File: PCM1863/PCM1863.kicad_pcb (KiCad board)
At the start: 2 copper layers, 70 x 45 mm, 47 parts, among them IC1 SN74AUC1G126DCKR, IC2 NCP163ASN330T1G, IC3 NCP163ASN330T1G, J1 Conn_01x10_Male, J2 Conn_01x10_Male, J3 Conn_01x10_Male, J4 USB_B_Micro, U1 PCM1863, Y1 ASE-24.000MHZ-ET, Y2 ASE-22.000MHZ-ET

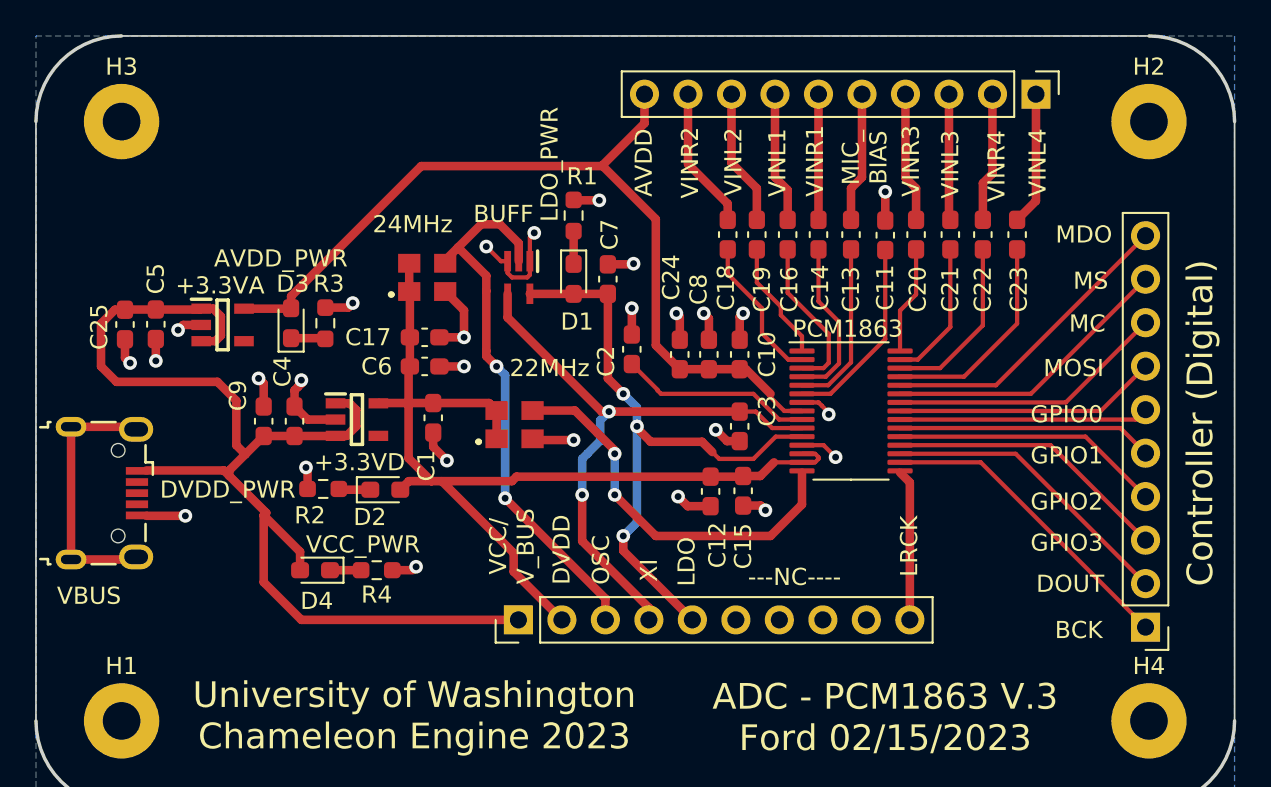
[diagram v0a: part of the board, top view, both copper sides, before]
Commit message: fix analog too close to digital
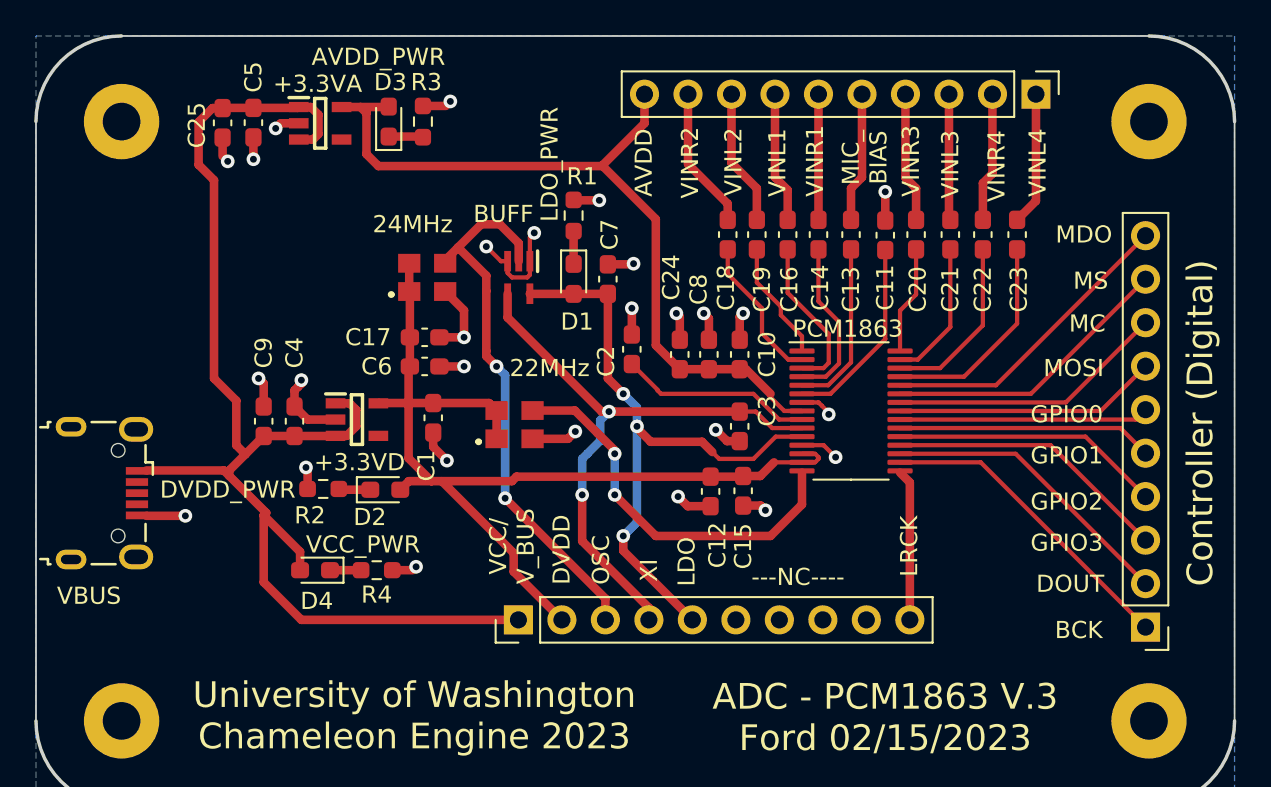
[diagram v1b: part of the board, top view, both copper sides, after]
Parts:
- moved C5 13.1 mm to (127.7, 120.1)
- moved D3 13.1 mm to (135.6, 120.0)
- moved IC3 13.1 mm to (131.6, 120.1)
- moved R3 13.1 mm to (137.6, 120.0)
- moved C25 13.1 mm to (125.9, 120.1)
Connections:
- J4 pad 6: unconnected-(J4-Pad6) -> GND
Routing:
- net unconnected-(J4-Pad6): track 15.3 -> 0.00 mm
- net VCC: track 67.7 -> 73.6 mm
- net AVDD: track 52.3 -> 47.3 mm

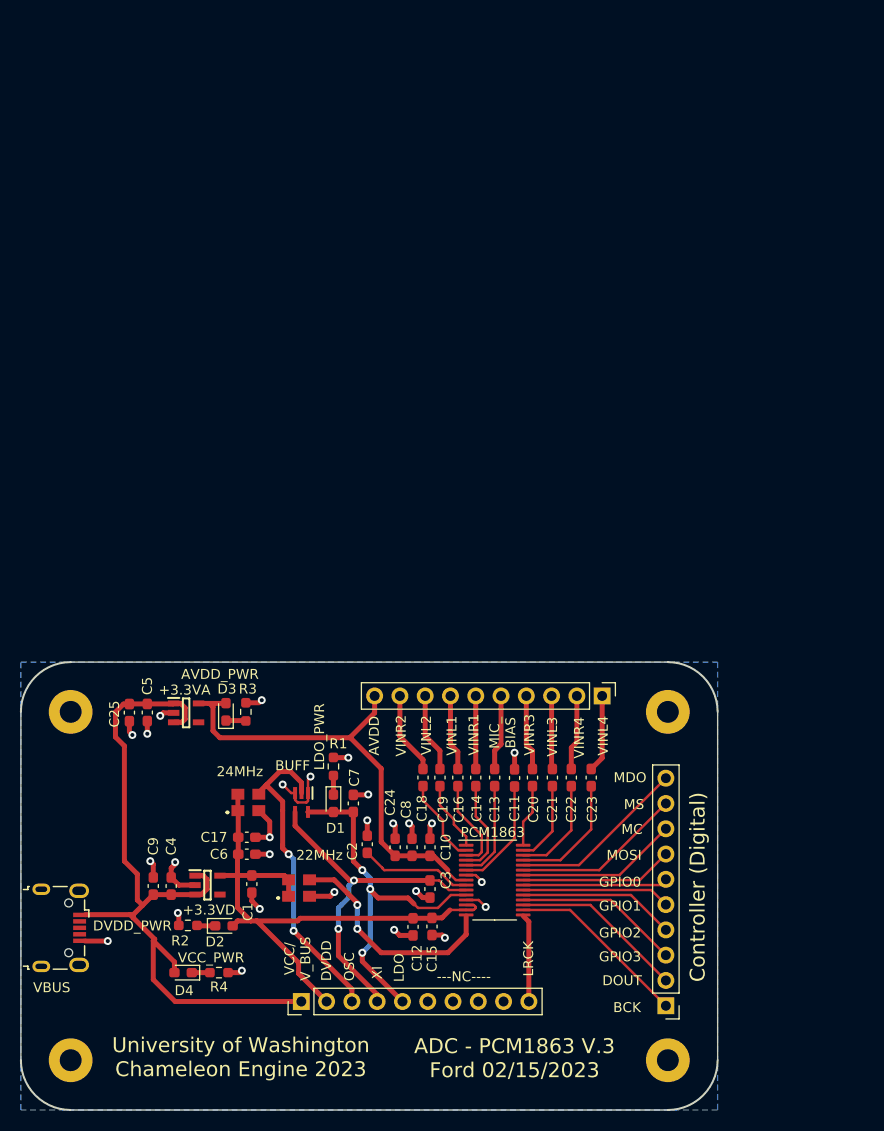
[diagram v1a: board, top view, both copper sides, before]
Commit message: schematic updates for ADC
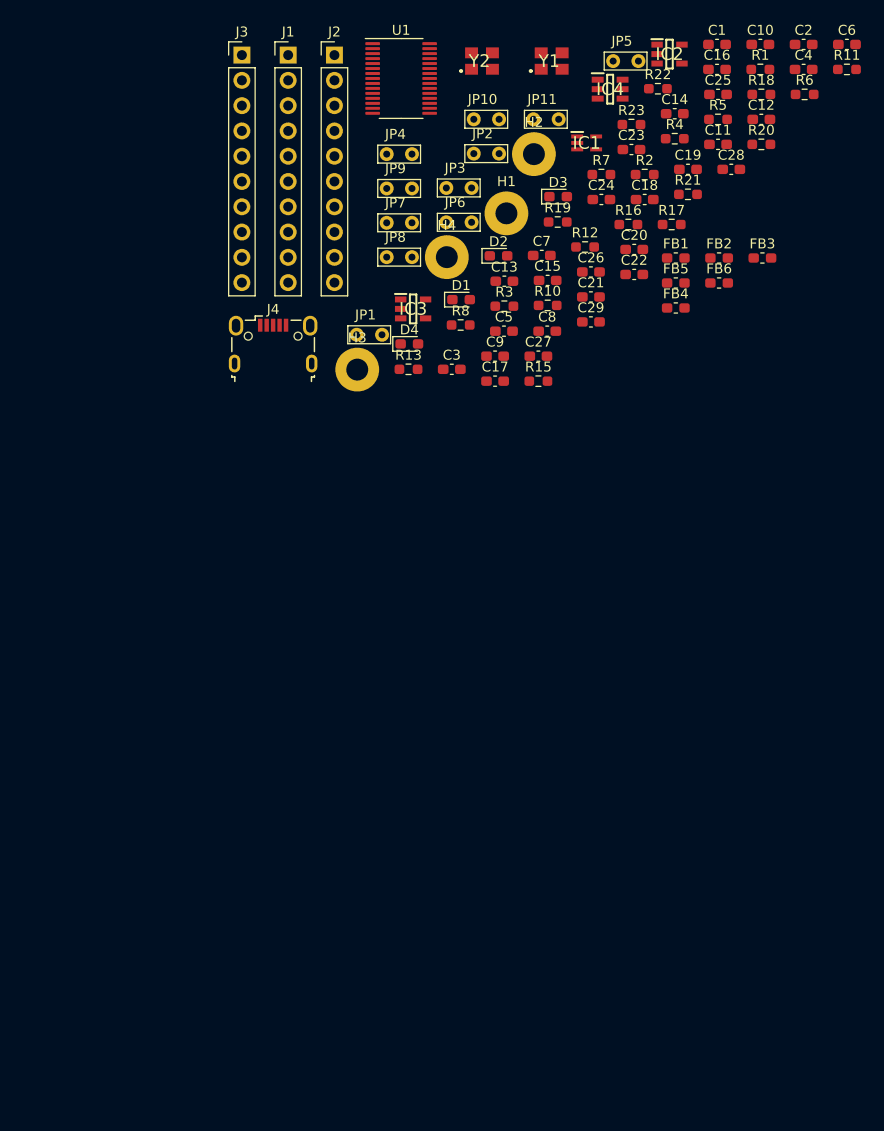
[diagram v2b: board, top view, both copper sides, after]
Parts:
- added C26: 10uF-16V, Capacitor_SMD:C_0603_1608Metric_Pad1.08x0.95mm_HandSolder, F.Cu at (172.3, 75.8)
- added C27: 10uF-16V, Capacitor_SMD:C_0603_1608Metric_Pad1.08x0.95mm_HandSolder, F.Cu at (167.0, 84.3)
- added C28: 0.1uF-16V, Capacitor_SMD:C_0603_1608Metric_Pad1.08x0.95mm_HandSolder, F.Cu at (186.4, 65.5)
- added C29: 0.1uF-16V, Capacitor_SMD:C_0603_1608Metric_Pad1.08x0.95mm_HandSolder, F.Cu at (172.3, 80.8)
- added FB1: FerriteBead, Inductor_SMD:L_0603_1608Metric_Pad1.05x0.95mm_HandSolder, F.Cu at (180.8, 74.4)
- added FB2: FerriteBead, Inductor_SMD:L_0603_1608Metric_Pad1.05x0.95mm_HandSolder, F.Cu at (185.2, 74.4)
- added FB3: FerriteBead, Inductor_SMD:L_0603_1608Metric_Pad1.05x0.95mm_HandSolder, F.Cu at (189.5, 74.4)
- added FB4: FerriteBead, Inductor_SMD:L_0603_1608Metric_Pad1.05x0.95mm_HandSolder, F.Cu at (180.8, 79.4)
- added FB5: FerriteBead, Inductor_SMD:L_0603_1608Metric_Pad1.05x0.95mm_HandSolder, F.Cu at (180.8, 76.9)
- added FB6: FerriteBead, Inductor_SMD:L_0603_1608Metric_Pad1.05x0.95mm_HandSolder, F.Cu at (185.2, 76.9)
- added IC4: TXB0101DBVT, custom_lib:SOT95P280X145-6N, F.Cu at (174.2, 57.4)
- added JP1: Jumper_2_Open, custom_lib:TestPoint_Bridge_Pitch2.54mm_Drill0.7mm, F.Cu at (147.5, 80.9)
- added JP10: Jumper_2_Open, custom_lib:TestPoint_Bridge_Pitch2.54mm_Drill0.7mm, F.Cu at (159.3, 59.3)
- added JP11: Jumper_2_Open, custom_lib:TestPoint_Bridge_Pitch2.54mm_Drill0.7mm, F.Cu at (165.3, 59.3)
- added JP2: Jumper_2_Open, custom_lib:TestPoint_Bridge_Pitch2.54mm_Drill0.7mm, F.Cu at (159.3, 62.7)
- added JP3: Jumper_2_Open, custom_lib:TestPoint_Bridge_Pitch2.54mm_Drill0.7mm, F.Cu at (156.5, 66.2)
- added JP4: Jumper_2_Open, custom_lib:TestPoint_Bridge_Pitch2.54mm_Drill0.7mm, F.Cu at (150.6, 62.8)
- added JP5: Jumper_2_Bridged, custom_lib:TestPoint_Bridge_Pitch2.54mm_Drill0.7mm, F.Cu at (173.3, 53.4)
- added JP6: Jumper_2_Open, custom_lib:TestPoint_Bridge_Pitch2.54mm_Drill0.7mm, F.Cu at (156.5, 69.6)
- added JP7: Jumper_2_Bridged, custom_lib:TestPoint_Bridge_Pitch2.54mm_Drill0.7mm, F.Cu at (150.6, 69.7)
- added JP8: Jumper_2_Open, custom_lib:TestPoint_Bridge_Pitch2.54mm_Drill0.7mm, F.Cu at (150.6, 73.1)
- added JP9: Jumper_2_Open, custom_lib:TestPoint_Bridge_Pitch2.54mm_Drill0.7mm, F.Cu at (150.6, 66.2)
- added R10: 2.2k, Resistor_SMD:R_0603_1608Metric_Pad0.98x0.95mm_HandSolder, F.Cu at (167.9, 79.2)
- added R11: 2.2k, Resistor_SMD:R_0603_1608Metric_Pad0.98x0.95mm_HandSolder, F.Cu at (198.0, 55.5)
- added R12: 100k, Resistor_SMD:R_0603_1608Metric_Pad0.98x0.95mm_HandSolder, F.Cu at (171.7, 73.3)
- added R13: 100k, Resistor_SMD:R_0603_1608Metric_Pad0.98x0.95mm_HandSolder, F.Cu at (153.9, 85.6)
- added R15: 2.2k, Resistor_SMD:R_0603_1608Metric_Pad0.98x0.95mm_HandSolder, F.Cu at (167.0, 86.8)
- added R16: 2.2k, Resistor_SMD:R_0603_1608Metric_Pad0.98x0.95mm_HandSolder, F.Cu at (176.0, 71.0)
- added R17: 100k, Resistor_SMD:R_0603_1608Metric_Pad0.98x0.95mm_HandSolder, F.Cu at (180.4, 71.0)
- added R18: 100k, Resistor_SMD:R_0603_1608Metric_Pad0.98x0.95mm_HandSolder, F.Cu at (189.4, 58.0)
- added R19: 2.2k, Resistor_SMD:R_0603_1608Metric_Pad0.98x0.95mm_HandSolder, F.Cu at (168.9, 70.8)
- added R20: 2.2k, Resistor_SMD:R_0603_1608Metric_Pad0.98x0.95mm_HandSolder, F.Cu at (189.4, 63.0)
- added R21: 100k, Resistor_SMD:R_0603_1608Metric_Pad0.98x0.95mm_HandSolder, F.Cu at (182.0, 68.0)
- added R22: 100k, Resistor_SMD:R_0603_1608Metric_Pad0.98x0.95mm_HandSolder, F.Cu at (179.0, 57.4)
- added R23: 4.99k, Resistor_SMD:R_0603_1608Metric_Pad0.98x0.95mm_HandSolder, F.Cu at (176.3, 61.0)
- added R5: 2.2k, Resistor_SMD:R_0603_1608Metric_Pad0.98x0.95mm_HandSolder, F.Cu at (185.0, 60.5)
- added R6: 2.2k, Resistor_SMD:R_0603_1608Metric_Pad0.98x0.95mm_HandSolder, F.Cu at (193.7, 58.0)
- added R7: 100k, Resistor_SMD:R_0603_1608Metric_Pad0.98x0.95mm_HandSolder, F.Cu at (173.3, 66.0)
- added R8: 100k, Resistor_SMD:R_0603_1608Metric_Pad0.98x0.95mm_HandSolder, F.Cu at (159.2, 81.1)
- C10, C15: value 0.1uF -> 0.1uF-16V
- C12, C14, C8: value 10uF -> 10uF-10V
- C13: value 0.1uF -> 0.1uF-50V
- C16: value 10uF -> 0.1uF-16V
- C18, C19, C20, C21, C22, C23: value 10uF -> 10uF-16V
- C2, C3: value 18pF -> 20pF-50V
- moved J3 104.6 mm to (137.2, 54.0), turned to 0 degrees
- moved C4 103.8 mm to (193.6, 55.5), turned to 0 degrees
- moved C6 101.3 mm to (198.0, 52.9), turned to 0 degrees
- moved C1 96.4 mm to (184.9, 52.9), turned to 0 degrees
- moved H1 95.7 mm to (163.8, 69.9)
- moved IC2 95.5 mm to (180.2, 53.9)
- moved R4 95.5 mm to (180.7, 62.4), turned to 0 degrees
- moved J1 95.1 mm to (141.9, 54.0), turned to 0 degrees
- moved C2 91.5 mm to (193.6, 52.9), turned to 0 degrees
- moved C12 88.4 mm to (189.4, 60.5), turned to 0 degrees
- moved R2 88.3 mm to (177.7, 66.0), turned to 0 degrees
- moved C10 87.2 mm to (189.3, 52.9), turned to 0 degrees
- moved C25 85.8 mm to (185.0, 58.0), turned to 0 degrees
- moved Y2 85.1 mm to (161.3, 54.6)
- moved H4 83.7 mm to (157.8, 74.3)
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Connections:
- C1 pad 2: GND -> GNDD
- C10 pad 1: GND -> GNDA
- C11 pad 1: GND -> GNDA
- C12 pad 2: GND -> GNDD
- C13 pad 1: /A5 -> GNDA
- C13 pad 2: Net-(C13-Pad2) -> MICBIAS
- C14 pad 1: /A4 -> LDO
- C14 pad 2: Net-(C14-Pad2) -> GNDD
- C15 pad 2: GND -> GNDD
- C16 pad 1: /A3 -> LDO
- C16 pad 2: Net-(C16-Pad2) -> GNDD
- C17 pad 2: GND -> GNDD
- C18 pad 1: /A2 -> VINR1
- C18 pad 2: Net-(C18-Pad2) -> /1R
- C19 pad 1: /A1 -> VINL1
- C19 pad 2: Net-(C19-Pad2) -> /1L
- C2 pad 1: GND -> GNDD
- C20 pad 1: /A17 -> VINR3
- C20 pad 2: Net-(C20-Pad2) -> /3R
- C21 pad 1: /A16 -> VINL3
- C21 pad 2: Net-(C21-Pad2) -> /3L
- C22 pad 1: /A15 -> VINR4
- C22 pad 2: Net-(C22-Pad2) -> /4R
- C23 pad 1: /A14 -> VINL4
- C23 pad 2: Net-(C23-Pad2) -> /4L
- C24 pad 1: GND -> GNDA
- C25 pad 2: GND -> GNDA
- C3 pad 1: GND -> GNDD
- C4 pad 2: GND -> GNDD
- C5 pad 2: GND -> GNDA
- C6 pad 1: GND -> GNDD
- C7 pad 2: GND -> GNDD
- C8 pad 1: GND -> GNDA
- C9 pad 2: GND -> GNDD
- IC1 pad 1: GND -> GNDD
- IC1 pad 3: GND -> GNDD
- IC2 pad 2: GND -> GNDD
- J1 pad 8: unconnected-(J1-Pad8) -> XO_BUFF
- J1 pad 9: unconnected-(J1-Pad9) -> SCKI(3.3V)
- J2 pad 1: /A14 -> /1R
- J2 pad 2: /A15 -> /1L
- J2 pad 3: /A16 -> /2R
- J2 pad 4: /A17 -> /2L
- J2 pad 5: /A5 -> /3R
- J2 pad 6: /A4 -> /3L
- J2 pad 7: /A3 -> /4R
- J2 pad 8: /A1 -> /4L
- J2 pad 9: /A2 -> MICBIAS
- J3 pad 10: /A13 -> /INT/GPIO3/INTC
- J3 pad 3: /A6 -> /MDO
- J3 pad 4: /A7 -> /MD1/MS/AD
- J3 pad 5: /A8 -> /MD3/MC/SCL
- J3 pad 6: /A9 -> /DOUT2/MD2/MOSI/SDA
- J3 pad 7: /A10 -> /MD4/MISO/GPIO0
- J3 pad 8: /A11 -> /MD5/GPIO1/INTA/DMIN
- J3 pad 9: /A12 -> /MD6/GPIO2/INTB/DMCLK
- J4 pad 5: GND -> GNDA
- J4 pad 6: GND -> unconnected-(J4-Pad6)
- R1 pad 2: GND -> GNDD
- R2 pad 2: GND -> GNDD
- R3 pad 2: GND -> GNDA
- R4 pad 1: GND -> GNDA
- U1 pad 1: Net-(C19-Pad2) -> /2L
- U1 pad 12: GND -> GNDD
- U1 pad 19: /A6 -> /INT/GPIO3/INTC
- U1 pad 2: Net-(C18-Pad2) -> /2R
- U1 pad 20: /A7 -> /MD6/GPIO2/INTB/DMCLK
- U1 pad 21: /A8 -> /MD5/GPIO1/INTA/DMIN
- U1 pad 22: /A9 -> /MD4/MISO/GPIO0
- U1 pad 23: /A10 -> /DOUT2/MD2/MOSI/SDA
- U1 pad 24: /A11 -> /MD3/MC/SCL
- U1 pad 25: /A12 -> /MD1/MS/AD
- U1 pad 26: /A13 -> /MDO
- U1 pad 27: Net-(C23-Pad2) -> /4L
- U1 pad 28: Net-(C22-Pad2) -> /4R
- U1 pad 29: Net-(C21-Pad2) -> /3L
- U1 pad 3: Net-(C16-Pad2) -> /1L
- U1 pad 30: Net-(C20-Pad2) -> /3R
- U1 pad 4: Net-(C14-Pad2) -> /1R
- U1 pad 5: Net-(C13-Pad2) -> MICBIAS
- U1 pad 7: GND -> GNDA
- Y1 pad 2: GND -> GNDD
- Y2 pad 2: GND -> GNDD
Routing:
- net VCC: track 73.6 -> 0.00 mm
- net DVDD: track 59.4 -> 0.00 mm
- net GND: track 53.7 -> 0.00 mm, vias 27 -> 0
- net AVDD: track 47.3 -> 0.00 mm
- net LDO: track 37.3 -> 0.00 mm, vias 3 -> 0
- net XI: track 35.7 -> 0.00 mm, vias 2 -> 0
- net OSC: track 32.2 -> 0.00 mm, vias 2 -> 0
- net SCKI(3.3V): track 22.9 -> 0.00 mm, vias 2 -> 0
- net BCK: track 18.3 -> 0.00 mm
- net /A13: track 18.0 -> 0.00 mm
- net DOUT: track 17.5 -> 0.00 mm
- net /A12: track 17.1 -> 0.00 mm
- net /A6: track 16.6 -> 0.00 mm
- net /A11: track 16.3 -> 0.00 mm
- net /A7: track 15.8 -> 0.00 mm
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- removed copper zone on B.Cu, net GND
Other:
- board outline removed
- board text removed: "+3.3VA"
- board text removed: "+3.3VD"
- board text removed: "---NC----"
- board text removed: "22MHz"
- board text removed: "24MHz"
- board text removed: "ADC - PCM1863 V.3 Ford 02/15/2023"
- board text removed: "AVDD"
- board text removed: "AVDD_PWR"
- board text removed: "BCK"
- board text removed: "BUFF"
- board text removed: "Controller (Digital)"
- board text removed: "DOUT"
- board text removed: "DVDD"
- board text removed: "DVDD_PWR"
- board text removed: "GPIO0"
- board text removed: "GPIO1"
- board text removed: "GPIO2"
- board text removed: "GPIO3"
- board text removed: "LDO"
- board text removed: "LDO_PWR"
- board text removed: "LRCK"
- board text removed: "MC"
- board text removed: "MDO"
- board text removed: "MIC_ BIAS"
- board text removed: "MOSI"
- board text removed: "MS"
- board text removed: "OSC"
- board text removed: "PCM1863"
- board text removed: "University of Washington Chameleon Engine 2023"
- board text removed: "VBUS"
- board text removed: "VCC/ V_BUS"
- board text removed: "VCC_PWR"
- board text removed: "VINL1"
- board text removed: "VINL2"
- board text removed: "VINL3"
- board text removed: "VINL4"
- board text removed: "VINR1"
- board text removed: "VINR2"
- board text removed: "VINR3"
- board text removed: "VINR4"
- board text removed: "XI"

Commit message: pcb grouping
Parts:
- moved R6 137.9 mm to (125.1, 177.6)
- moved R11 134.8 mm to (139.9, 177.1)
- moved R18 125.2 mm to (150.3, 176.9)
- moved R22 124.3 mm to (161.4, 180.5)
- moved JP4 121.2 mm to (137.8, 183.3)
- moved JP2 121.0 mm to (126.9, 179.3)
- moved R20 119.8 mm to (166.0, 180.5)
- moved JP11 115.5 mm to (159.5, 174.6)
- moved R16 114.5 mm to (150.9, 182.7)
- moved J2 114.2 mm to (158.7, 167.6), turned to -90 degrees
- moved C23 112.4 mm to (184.1, 175.6)
- moved JP9 112.3 mm to (148.1, 178.5)
- moved R5 112.0 mm to (133.1, 159.7)
- moved R7 105.4 mm to (128.8, 161.6)
- moved R4 101.8 mm to (90.9, 110.4)
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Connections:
- C1 pad 2: GNDD -> GND
- C12 pad 2: GNDD -> GND
- C14 pad 2: GNDD -> GND
- C15 pad 2: GNDD -> GND
- C16 pad 2: GNDD -> GND
- C17 pad 2: GNDD -> GND
- C2 pad 1: GNDD -> GND
- C28 pad 2: GNDD -> GND
- C29 pad 1: GNDD -> GND
- C3 pad 1: GNDD -> GND
- C4 pad 2: GNDD -> GND
- C6 pad 1: GNDD -> GND
- C7 pad 2: GNDD -> GND
- C9 pad 2: GNDD -> GND
- FB1 pad 1: GNDD -> GND
- FB2 pad 1: GNDD -> GND
- FB3 pad 1: GNDD -> GND
- FB4 pad 2: GNDD -> GND
- FB5 pad 2: GNDD -> GND
- FB6 pad 2: GNDD -> GND
- IC1 pad 1: GNDD -> GND
- IC1 pad 3: GNDD -> GND
- IC2 pad 2: GNDD -> GND
- IC4 pad 2: GNDD -> GND
- JP5 pad 2: GNDD -> GND
- JP6 pad 2: GNDD -> GND
- R1 pad 2: GNDD -> GND
- R2 pad 2: GNDD -> GND
- U1 pad 12: GNDD -> GND
- Y1 pad 2: GNDD -> GND
- Y2 pad 2: GNDD -> GND
